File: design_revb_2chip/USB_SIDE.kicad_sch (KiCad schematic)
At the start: 2 parts, among them J1 USB_C_Receptacle, U1 LAN7801-I/9JX

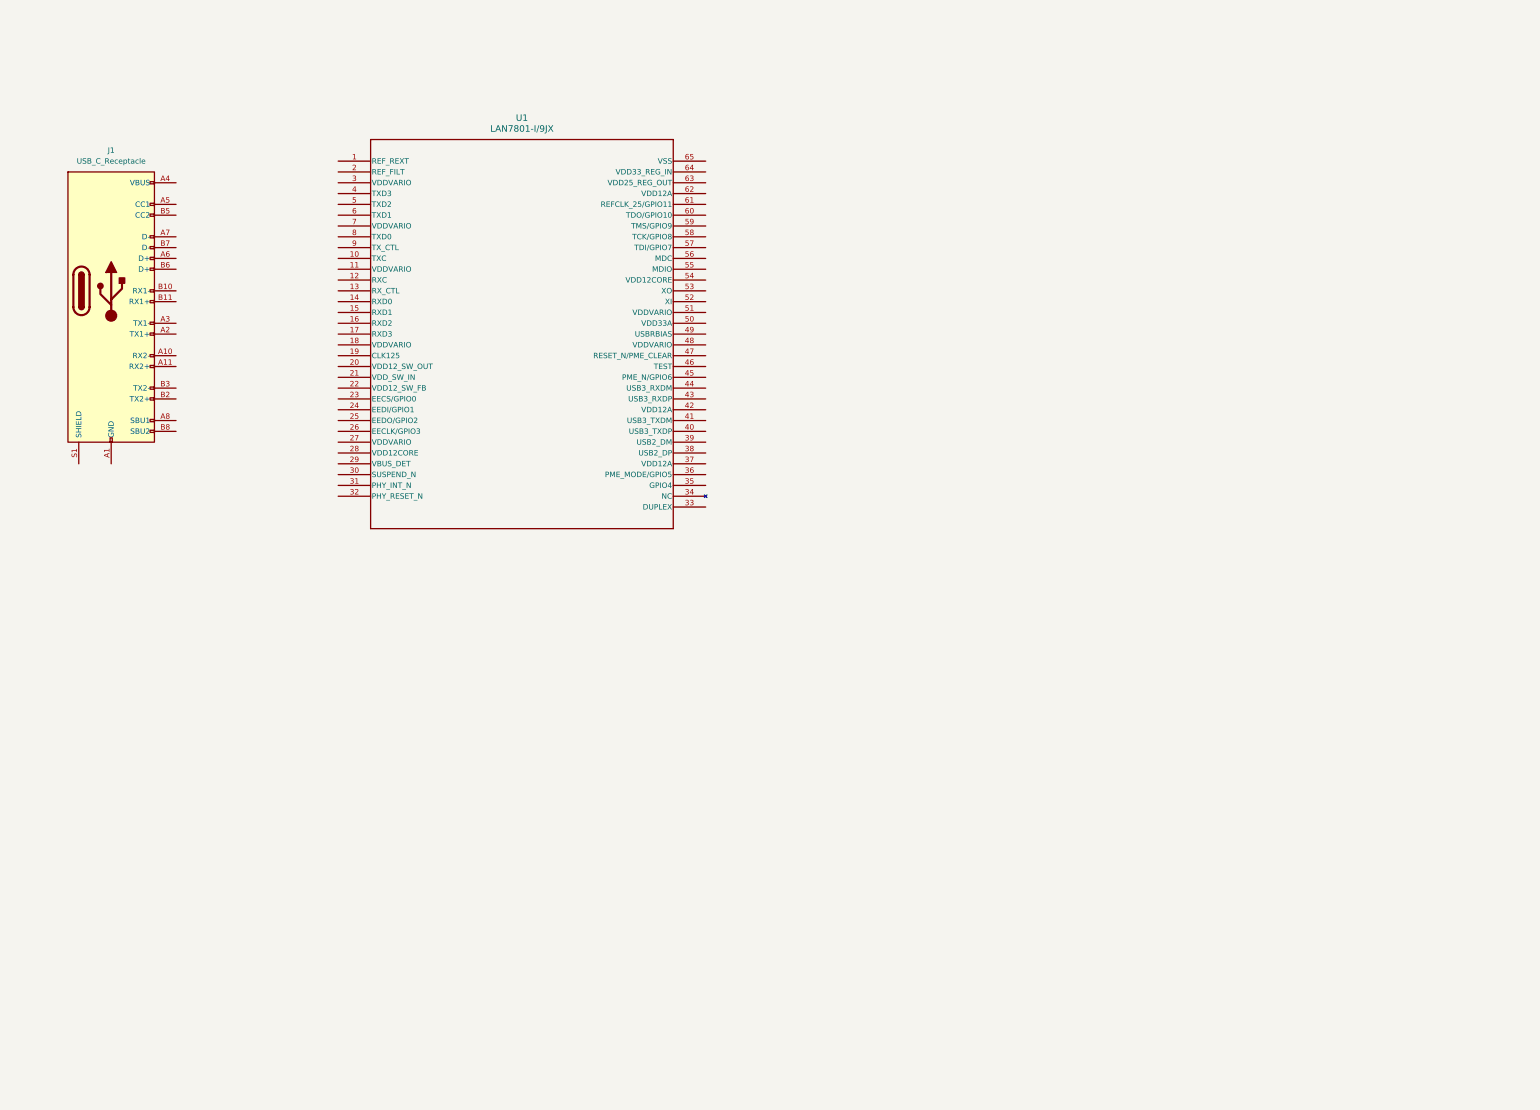
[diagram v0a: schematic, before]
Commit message: USB Side Progress 1
- EEPROM done
- data components done
- some power components done
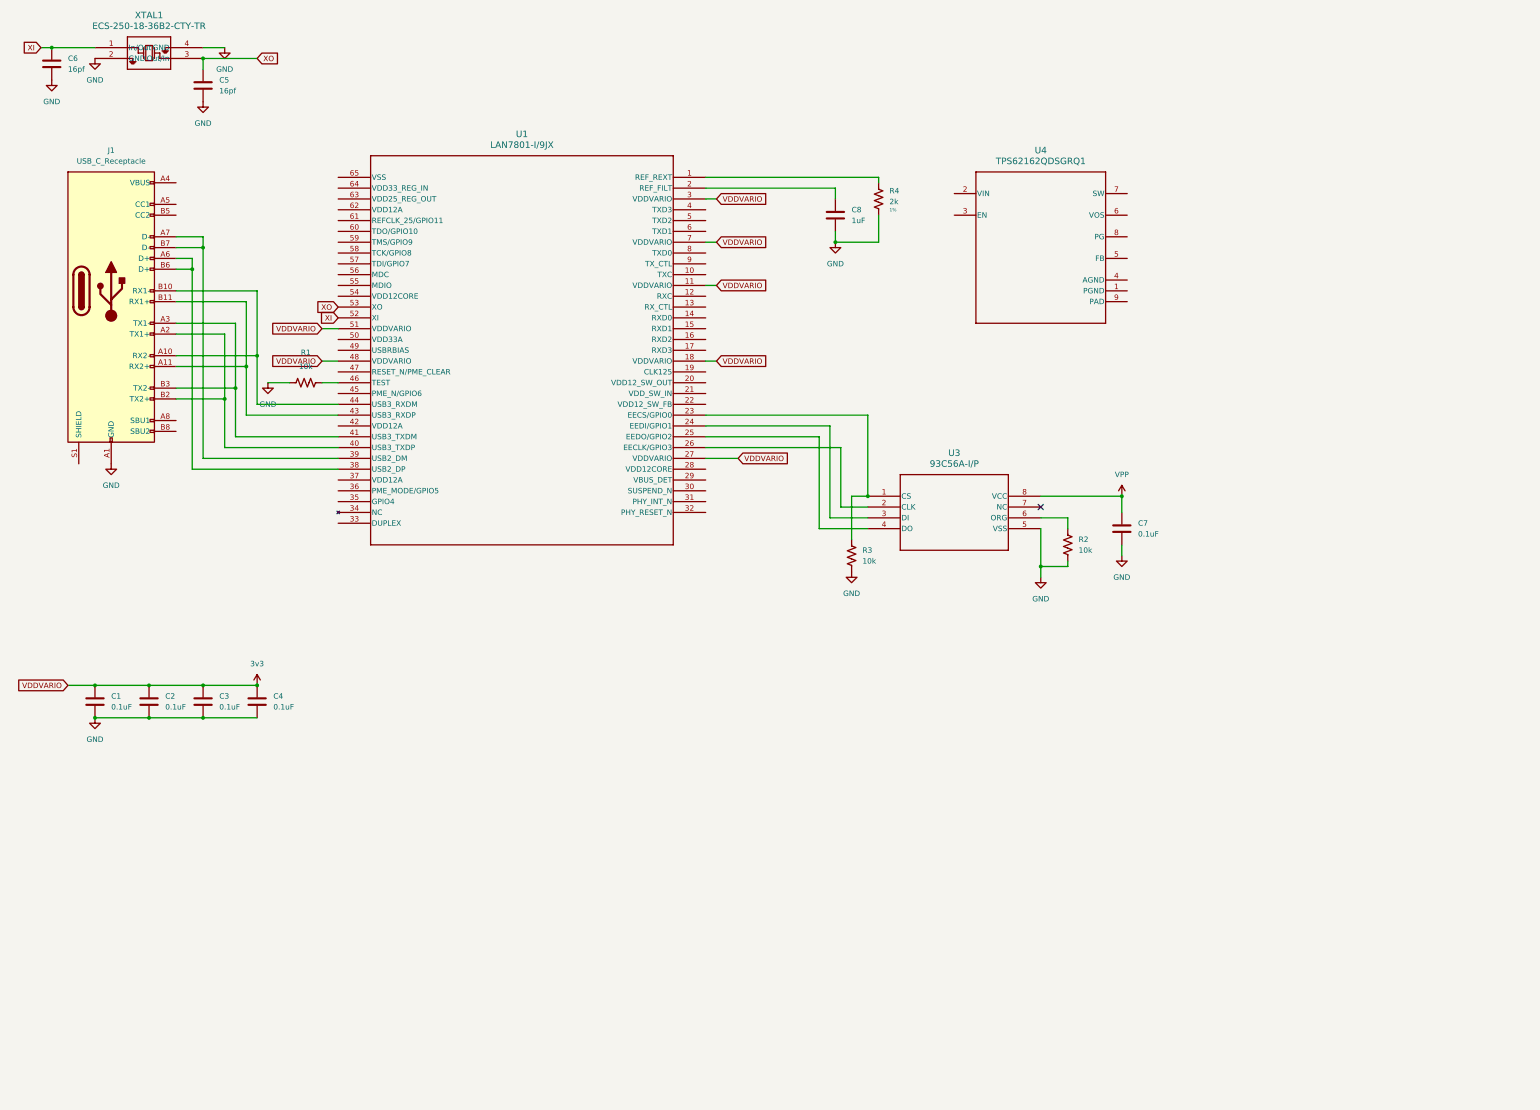
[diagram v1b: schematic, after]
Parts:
- added C1, C2, C3, C4, C7: 0.1uF, symbol Device:C
- added C5, C6: 16pf, symbol Device:C
- added C8: 1uF, symbol Device:C
- added R1, R2, R3: 10k, symbol Device:R_US
- added R4: 2k, symbol Device:R_US
- added U3: 93C56A-I/P, PDIP8_300MC_MCH, symbol Capstone_Synbols:93C56A-I_P
- added U4: TPS62162QDSGRQ1, DSG0008A, symbol Capstone_Synbols:TPS62162QDSGRQ1
- added XTAL1: ECS-250-18-36B2-CTY-TR, ECX-2236B2_ECS, symbol Capstone_Synbols:ECS-250-18-36B2-CTY-TR
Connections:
- net GND: now reaches J1.A1 (GND), J1.A12 (GND), J1.B1 (GND), J1.B12 (GND)
- net GND: now also C1.2, C2.2, C3.2, C4.2, C5.2, C6.2, C7.2, C8.2, R1.1, R2.1, R3.1, R4.1, U3.5 (VSS), XTAL1.2 (GND), XTAL1.4 (GND)
- net at J1.A10 (RX2-): now also J1.B10 (RX1-), U1.44 (USB3_RXDM)
- net at J1.A11 (RX2+): now also J1.B11 (RX1+), U1.43 (USB3_RXDP)
- net at J1.A2 (TX1+): now also J1.B2 (TX2+), U1.40 (USB3_TXDP)
- net at J1.A3 (TX1-): now also J1.B3 (TX2-), U1.41 (USB3_TXDM)
- net at J1.A6 (D+): now also J1.B6 (D+), U1.38 (USB2_DP)
- net at J1.A7 (D-): now also J1.B7 (D-), U1.39 (USB2_DM)
- net at U1.1 (REF_REXT): now also R4.2
- net 3v3: now reaches U1.11 (VDDVARIO)
- net 3v3: now also U1.18 (VDDVARIO), U1.27 (VDDVARIO), U1.3 (VDDVARIO), U1.48 (VDDVARIO), U1.51 (VDDVARIO), U1.7 (VDDVARIO), C1.1, C2.1, C3.1, C4.1
- net at U1.2 (REF_FILT): now also C8.1
- net at U1.23 (EECS/GPIO0): now also R3.2, U3.1 (CS)
- net at U1.24 (EEDI/GPIO1): now also U3.3 (DI)
- net at U1.25 (EEDO/GPIO2): now also U3.4 (DO)
- net at U1.26 (EECLK/GPIO3): now also U3.2 (CLK)
- net at U1.46 (TEST): now also R1.2
- net XI: now reaches U1.52 (XI)
- net XI: now also C6.1, XTAL1.1 (In/Out)
- net XO: now reaches U1.53 (XO)
- net XO: now also C5.1, XTAL1.3 (Out/In)
- new net: R2.2, U3.6 (ORG)
- new net VPP: C7.1, U3.8 (VCC)
- no-connect marks 0 -> 1
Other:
- moved on the sheet: U1

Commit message: Roughly Finishes
First Draft of Completed USB-Side Schematic
- LAN7801 connections
- Regulator
- Oscillator
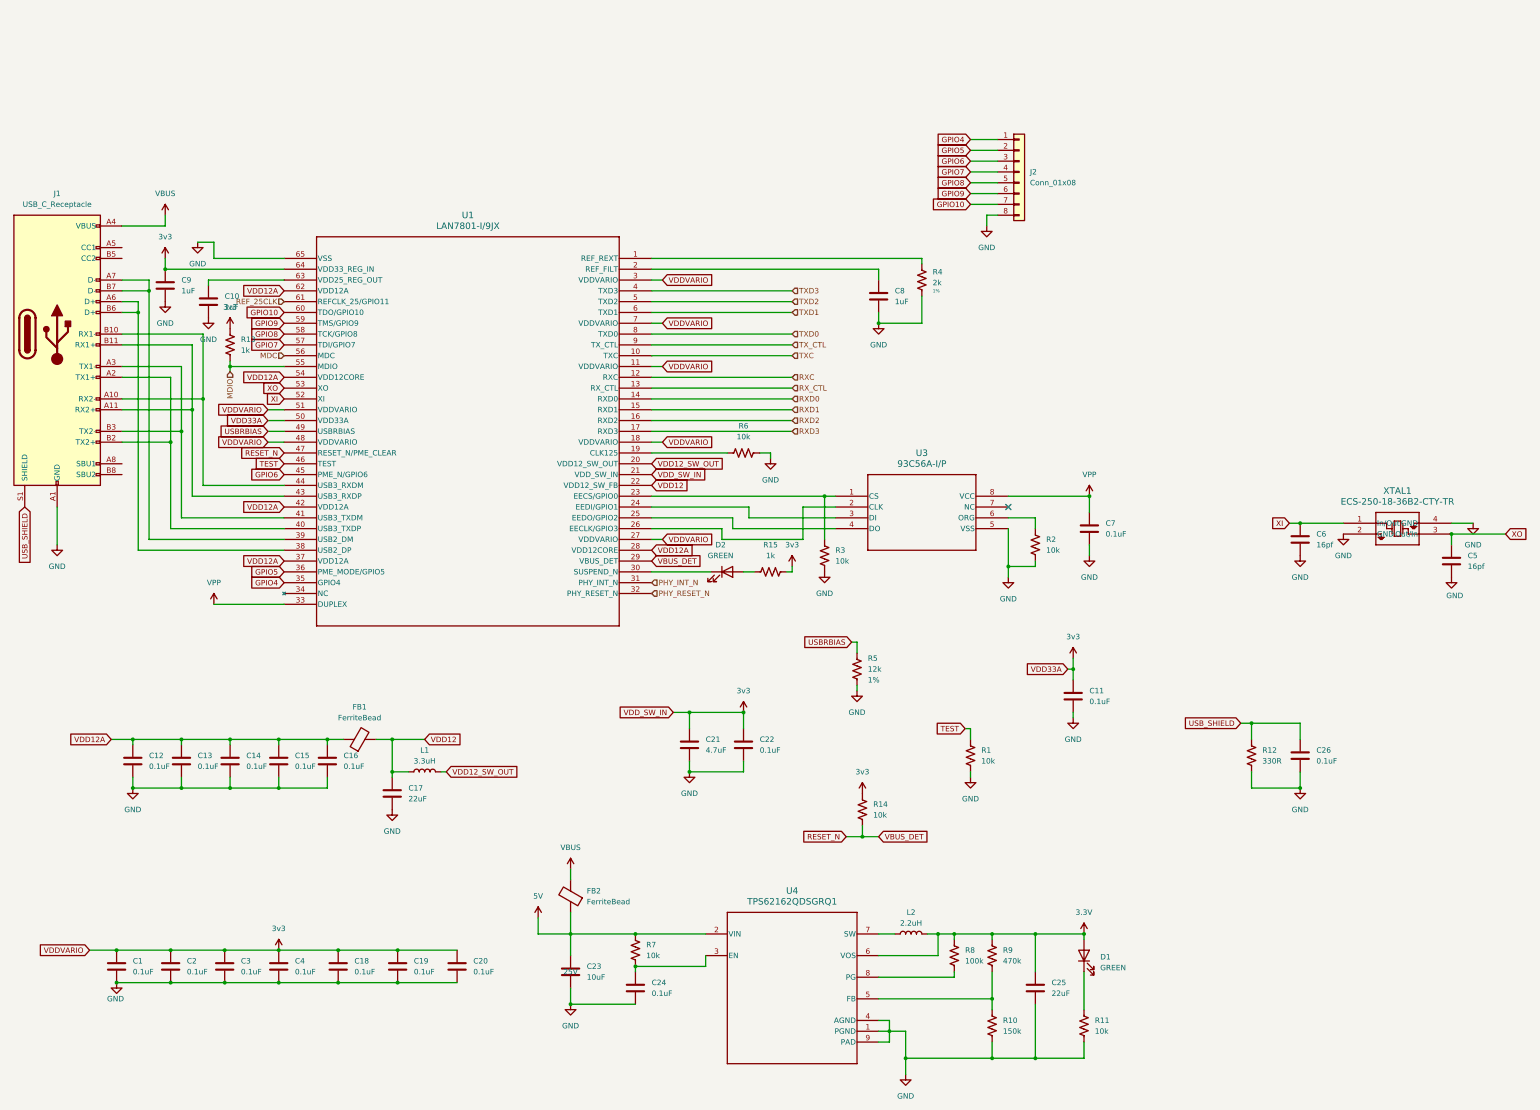
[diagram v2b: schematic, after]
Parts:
- added C10, C9: 1uF, symbol Device:C
- added C11, C12, C13, C14, C15, C16, C18, C19, C20, C22, C24, C26: 0.1uF, symbol Device:C
- added C17, C25: 22uF, symbol Device:C
- added C21: 4.7uF, symbol Device:C
- added C23: 10uF, symbol Device:C
- added D1, D2: GREEN, symbol Device:LED
- added FB1, FB2: FerriteBead, symbol Device:FerriteBead
- added J2: Conn_01x08, symbol Connector_Generic:Conn_01x08
- added L1: 3.3uH, symbol Device:L
- added L2: 2.2uH, symbol Device:L
- added R10: 150k, symbol Device:R_US
- added R11, R14, R6, R7: 10k, symbol Device:R_US
- added R12: 330R, symbol Device:R_US
- added R13, R15: 1k, symbol Device:R_US
- added R5: 12k, symbol Device:R_US
- added R8: 100k, symbol Device:R_US
- added R9: 470k, symbol Device:R_US
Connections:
- net 3v3: now also U1.21 (VDD_SW_IN), U1.50 (VDD33A), U1.64 (VDD33_REG_IN), C11.1, C18.1, C19.1, C20.1, C21.1, C22.1, C9.1, R13.2, R14.2, R15.1
- net GND: now also U1.65 (VSS), U4.1 (PGND), U4.4 (AGND), U4.9 (PAD), C10.2, C11.2, C12.2, C13.2, C14.2, C15.2, C16.2, C17.2, C18.2, C19.2, C20.2, C21.2, C22.2, C23.2, C24.2, C25.2, C26.2, C9.2, J2.8 (Pin_8), R10.1, R11.1, R12.1, R5.1, R6.1
- net VPP: now also U1.33 (DUPLEX)
- net TEST: now reaches R1.2, U1.46 (TEST)
- net 5V: now reaches U4.2 (VIN)
- net 5V: now also C23.1, FB2.1, R7.2
- net at U4.3 (EN): now also C24.1, R7.1
- net at U4.5 (FB): now also R10.2, R9.1
- net 3.3V: now reaches U4.6 (VOS)
- net 3.3V: now also C25.1, D1.2 (A), L2.2, R8.2, R9.2
- net at U4.7 (SW): now also L2.1
- net at U4.8 (PG): now also R8.1
- net VBUS: now reaches J1.A4 (VBUS), J1.A9 (VBUS), J1.B4 (VBUS), J1.B9 (VBUS)
- net VBUS: now also FB2.2
- net USB_SHIELD: now reaches J1.S1 (SHIELD)
- net USB_SHIELD: now also C26.1, R12.2
- net TXC: now reaches U1.10 (TXC)
- net RXC: now reaches U1.12 (RXC)
- net RX_CTL: now reaches U1.13 (RX_CTL)
- net RXD0: now reaches U1.14 (RXD0)
- net RXD1: now reaches U1.15 (RXD1)
- net RXD2: now reaches U1.16 (RXD2)
- net RXD3: now reaches U1.17 (RXD3)
- net at U1.19 (CLK125): now also R6.2
- net VDD12_SW_OUT: now reaches U1.20 (VDD12_SW_OUT)
- net VDD12_SW_OUT: now also L1.2
- net VDD12: now reaches U1.22 (VDD12_SW_FB)
- net VDD12: now also C17.1, FB1.2, L1.1
- net VDD12A: now reaches U1.28 (VDD12CORE)
- net VDD12A: now also U1.37 (VDD12A), U1.42 (VDD12A), U1.54 (VDD12CORE), U1.62 (VDD12A), C12.1, C13.1, C14.1, C15.1, C16.1, FB1.1
- net RESET_N: now reaches U1.29 (VBUS_DET)
- net RESET_N: now also U1.47 (RESET_N/PME_CLEAR), R14.1
- net at U1.30 (SUSPEND_N): now also D2.1 (K)
- net PHY_INT_N: now reaches U1.31 (PHY_INT_N)
- net PHY_RESET_N: now reaches U1.32 (PHY_RESET_N)
- net GPIO4: now reaches U1.35 (GPIO4)
- net GPIO4: now also J2.1 (Pin_1)
- net GPIO5: now reaches U1.36 (PME_MODE/GPIO5)
- net GPIO5: now also J2.2 (Pin_2)
- net TXD3: now reaches U1.4 (TXD3)
- net GPIO6: now reaches U1.45 (PME_N/GPIO6)
- net GPIO6: now also J2.3 (Pin_3)
- net USBRBIAS: now reaches U1.49 (USBRBIAS)
- net USBRBIAS: now also R5.2
- net TXD2: now reaches U1.5 (TXD2)
- net MDIO: now reaches U1.55 (MDIO)
- net MDIO: now also R13.1
- net MDC: now reaches U1.56 (MDC)
- net GPIO7: now reaches U1.57 (TDI/GPIO7)
- net GPIO7: now also J2.4 (Pin_4)
- net GPIO8: now reaches U1.58 (TCK/GPIO8)
- net GPIO8: now also J2.5 (Pin_5)
- net GPIO9: now reaches U1.59 (TMS/GPIO9)
- net GPIO9: now also J2.6 (Pin_6)
- net TXD1: now reaches U1.6 (TXD1)
- net GPIO10: now reaches U1.60 (TDO/GPIO10)
- net GPIO10: now also J2.7 (Pin_7)
- net REF_25CLK: now reaches U1.61 (REFCLK_25/GPIO11)
- net at U1.63 (VDD25_REG_OUT): now also C10.1
- net TXD0: now reaches U1.8 (TXD0)
- net TX_CTL: now reaches U1.9 (TX_CTL)
- new net: D2.2 (A), R15.2
- new net: D1.1 (K), R11.2
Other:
- moved on the sheet: C1, C2, C3, C4, C5, C6, C7, C8, J1, R1, R2, R3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

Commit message: Annotation
Quick Annotation Update before PCB
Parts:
- renumbered C4 to C10, C16 to C11, C18 to C12, C17 to C13, C19 to C14, C20 to C15, C23 to C16, C24 to C17, C21 to C18, C22 to C19, C12 to C2, C8 to C20, C25 to C21, C11 to C22, C7 to C23, C6 to C24, C26 to C25, C5 to C26, C9 to C3, C2 to C4, C13 to C5, C10 to C6, C3 to C7, C14 to C8, C15 to C9, D2 to D1, D1 to D2, R13 to R1, R1 to R10, R9 to R11, R10 to R12, R2 to R13, R11 to R14, R12 to R15, R7 to R2, R6 to R3, R15 to R4, R3 to R5, R5 to R6, R14 to R7, R4 to R8, R8 to R9, U4 to U2
